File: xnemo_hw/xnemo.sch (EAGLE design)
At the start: 40 parts, among them J1 MICRO_USB_B_RECEPT, J2 DM3D_MICRO_SD, J3 HEADER_2X5_0.05_SMD, J4 HEADER_2X5_0.05_THRU, J5 HEADER_2X5_0.05_THRU, U1 LTC3559, U2 L3GD20, U3 STM32F405RG, U4 STM32F407VE, U5 HMC5883L, U6 ADXL345, X1 TXC_7A_XTAL

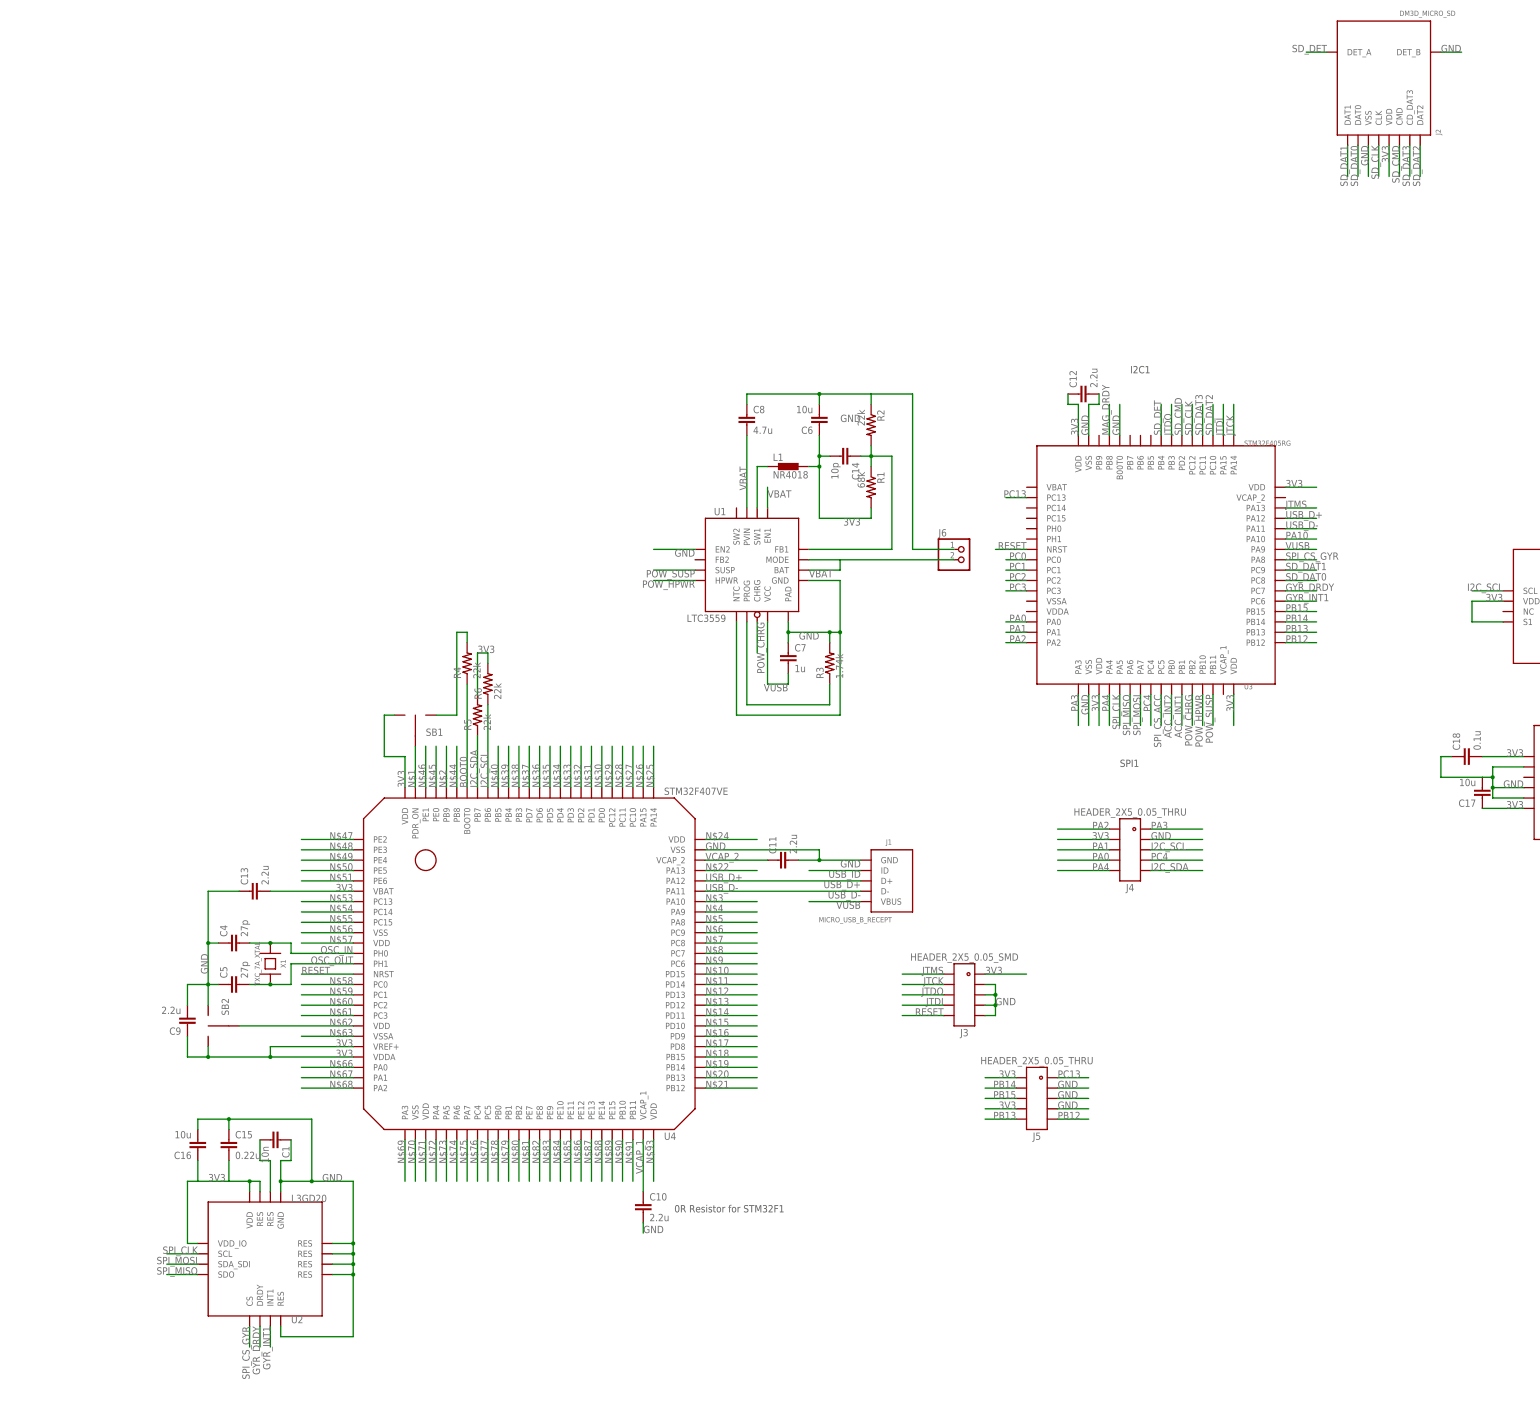
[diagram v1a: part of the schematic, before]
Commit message: More junk added -- 2 compass units...
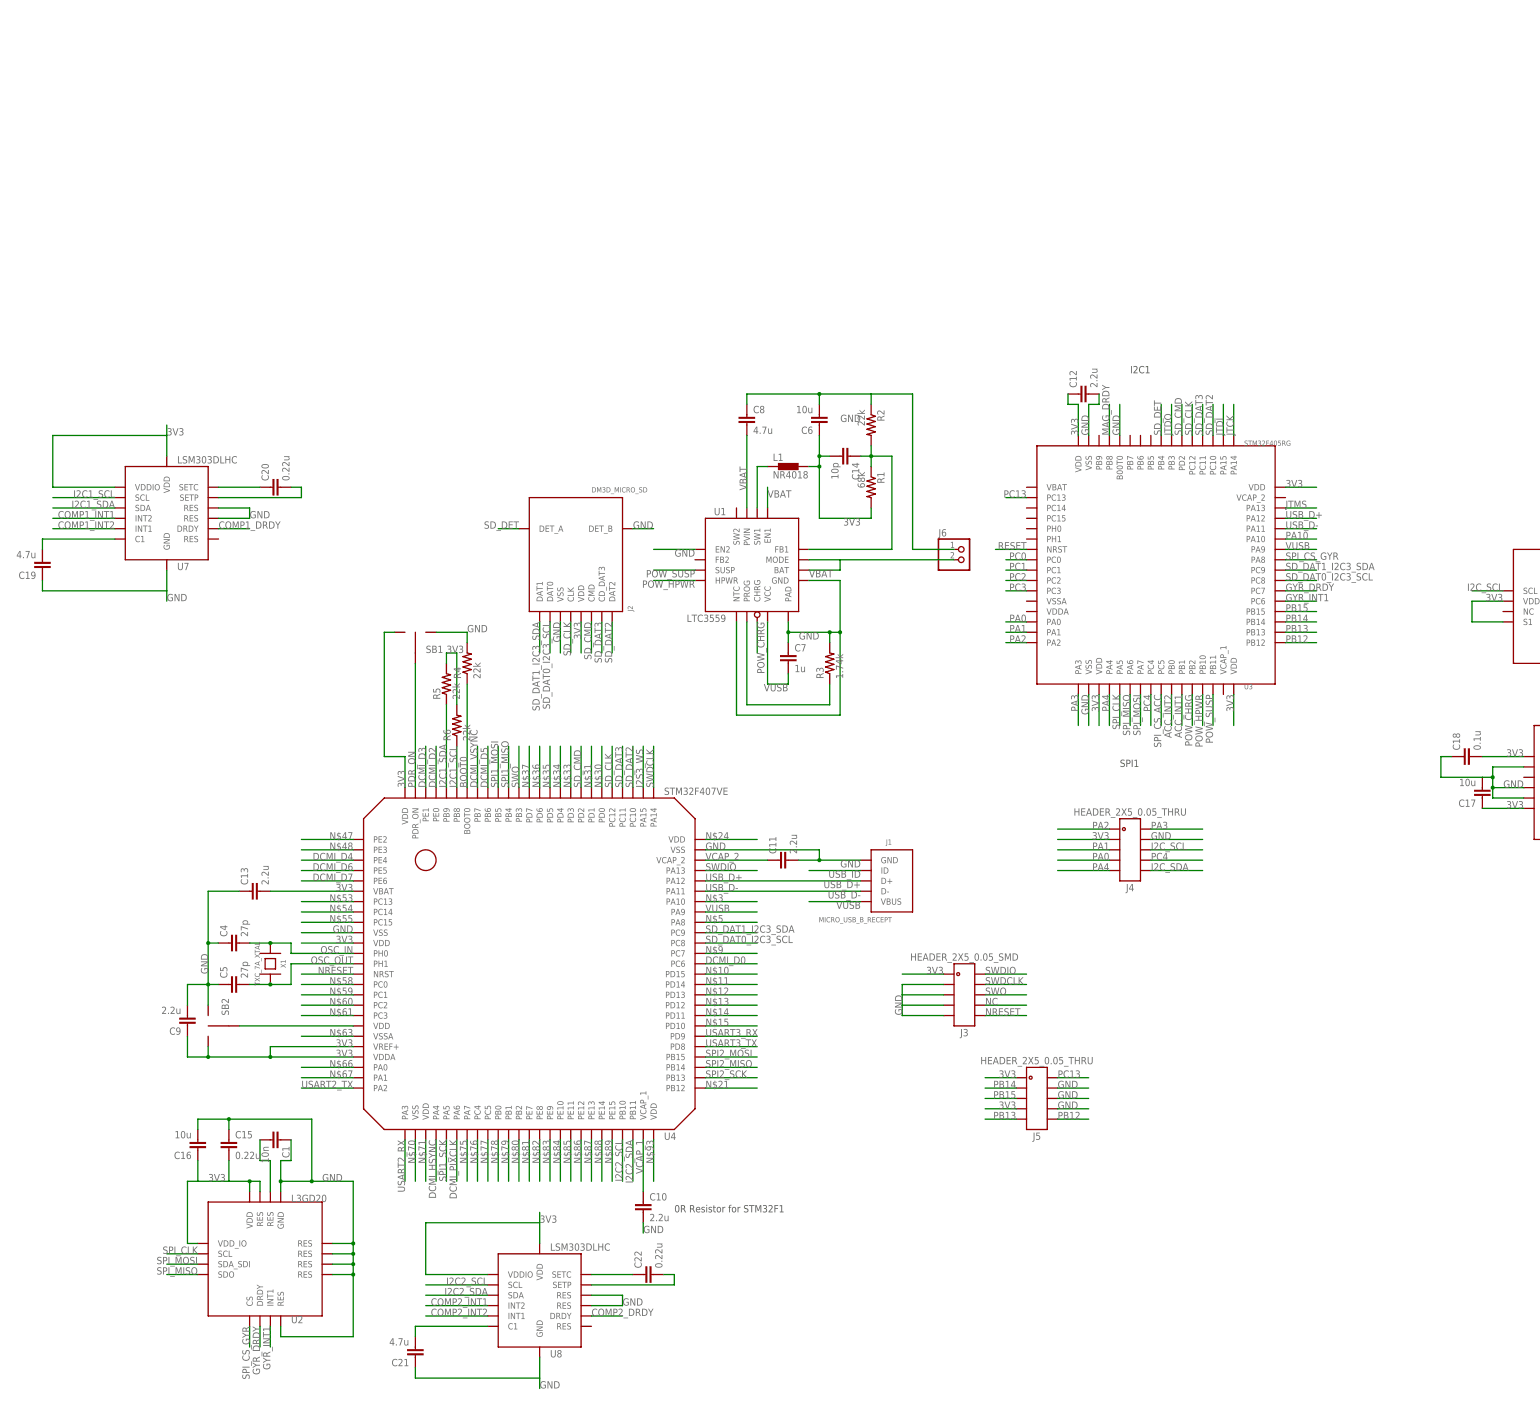
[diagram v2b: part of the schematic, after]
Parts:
- added C19, C21: 4.7u, resistor:C-EUC0805
- added C20, C22: 0.22u, resistor:C-EUC0402
- added U7, U8: LSM303DLHC, xnemo:LSM303DLHC
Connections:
- net N$1 renamed PDR_ON
- net N$16 renamed USART3_RX
- net N$17 renamed USART3_TX
- net N$18 renamed SPI2_MOSI
- net N$19 renamed SPI2_MISO
- net N$20 renamed SPI2_SCK
- net N$26 renamed I2S3_WS
- net N$39 renamed SPI1_MISO
- net N$40 renamed SPI1_MOSI
- net N$45 renamed DCMI_D2
- net N$46 renamed DCMI_D3
- net N$49 renamed DCMI_D4
- net N$50 renamed DCMI_D6
- net N$51 renamed DCMI_D7
- net N$68 renamed USART2_TX
- net N$69 renamed USART2_RX
- net N$72 renamed DCMI_HSYNC
- net N$73 renamed SPI1_SCK
- net N$74 renamed DCMI_PIXCLK
- net N$9 renamed DCMI_D0
- removed net N$2: U4.PB9
- removed net N$22: U4.PA13
- removed net N$25: U4.PA14
- removed net N$29: U4.PC12
- removed net N$32: U4.PD2
- removed net N$38: U4.PB3
- removed net N$4: U4.PA9
- removed net N$44: U4.PB8
- removed net N$56: U4.VSS@1
- removed net N$57: U4.VDD@1
- removed net N$90: U4.PB10
- removed net N$91: U4.PB11
- removed net SD_DAT0: J2.DAT0, U3.PC8
- removed net SD_DAT1: J2.DAT1, U3.PC9
- new net COMP1_DRDY: U7.DRDY
- new net COMP1_INT1: U7.INT2
- new net COMP1_INT2: U7.INT1
- new net COMP2_DRDY: U8.DRDY
- new net COMP2_INT1: U8.INT2
- new net COMP2_INT2: U8.INT1
- new net DCMI_D5: U4.PB6
- new net DCMI_VSYNC: U4.PB7
- new net I2C1_SCL: R6.1, U4.PB8, U7.SCL
- new net I2C1_SDA: R5.1, U4.PB9, U7.SDA
- new net I2C2_SCL: U4.PB10, U8.SCL
- new net I2C2_SDA: U4.PB11, U8.SDA
- new net N$23: C22.1, U8.SETC
- new net N$52: C19.2, U7.C1
- new net NC: J3.7
- new net NRESET: J3.9, U4.NRST
- new net SD_DAT0_I2C3_SCL: J2.DAT0, U3.PC8, U4.PC8
- new net SD_DAT1_I2C3_SDA: J2.DAT1, U3.PC9, U4.PC9
- new net SWDCLK: J3.3, U4.PA14
- new net SWDIO: J3.1, U4.PA13
- new net SWO: J3.5, U4.PB3
- net 3V3: now also J3.2, U4.VDD@1, U7.VDD, U7.VDDIO, U8.VDD, U8.VDDIO; no longer J3.1
- net GND: now also C19.1, C21.1, J3.10, J3.4, J3.6, J3.8, U4.VSS@1, U7.GND, U7.RES@2, U7.RES@3, U8.GND, U8.RES@2, U8.RES@3; no longer J3.3, J3.5, J3.7, J3.9
- net I2C_SCL: no longer R6.1, U4.PB6
- net I2C_SDA: no longer R5.1, U4.PB7
- net JTCK: no longer J3.4
- net JTDI: no longer J3.8
- net JTDO: no longer J3.6
- net JTMS: no longer J3.2
- net N$27: now also C20.1, U7.SETC; no longer U4.PC10
- net N$28: now also C21.2, U8.C1; no longer U4.PC11
- net N$6: now also C22.2, U8.SETP; no longer U4.PC9
- net N$7: now also C20.2, U7.SETP; no longer U4.PC8
- net RESET: no longer J3.10, U4.NRST
- net SD_CLK: now also U4.PC12
- net SD_CMD: now also U4.PD2
- net SD_DAT2: now also U4.PC10
- net SD_DAT3: now also U4.PC11
- net VUSB: now also U4.PA9
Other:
- moved on the sheet: J2, R5, R6, SB1

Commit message: Started routing
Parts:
- removed C18: 0.1u, resistor:C-EUC0402
- removed J5: HEADER_2X5_0.05_THRU, xnemo:HEADER_2X5_0.05_THRU
- removed U3: STM32F405RG, xnemo:STM32F405RG
- removed U5: HMC5883L, xnemo:HMC5883L
- removed U6: ADXL345, xnemo:ADXL345
- added C23: 10n, resistor:C-EUC0402
- added C24: 0.22u, resistor:C-EUC0402
- added C25: 10u, resistor:C-EUC0805
- added R7: 33k, resistor:R-US_R0402
- added R8, R9: 22k, resistor:R-US_R0402
- added U10: STTS751, xnemo:STTS751
- added U9: L3GD20, xnemo:L3GD20
- C17: value 10u -> 2.2u; device resistor:C-EUC0805 -> resistor:C-EUC0603
- C2: value 0.22u -> 10u; device resistor:C-EUC0402 -> resistor:C-EUC0805
- C3: value 4.7u -> 2.2u; device resistor:C-EUC0805 -> resistor:C-EUC0603
- J4: value HEADER_2X5_0.05_THRU -> HEADER_2X7; device xnemo:HEADER_2X5_0.05_THRU -> xnemo:HEADER_2X7
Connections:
- net GYR_RES renamed GYR_RES1
- net N$21 renamed SPI2_NSS_WS
- net N$28 renamed COMP2_C1
- net N$52 renamed COMP1_C1
- net SPI2_MISO renamed SPI2_MISO_EXT_SD
- net SPI2_MOSI renamed SPI2_MOSI_SD
- net SPI2_SCK renamed SPI2_SCK_CK
- removed net ACC_INT1: U3.PB1, U6.INT1
- removed net ACC_INT2: U3.PB0, U6.INT2
- removed net DCMI_D0: U4.PC6
- removed net GYR_DRDY: U2.DRDY, U3.PC7
- removed net GYR_INT1: U2.INT1, U3.PC6
- removed net I2C_SCL: J4.5, U5.SCL
- removed net I2C_SDA: J4.9, U5.SDA
- removed net JTCK: U3.PA14
- removed net JTDI: U3.PA15
- removed net JTDO: U3.PB3
- removed net JTMS: U3.PA13
- removed net MAG_C1: C3.1, U5.C1
- removed net MAG_DRDY: U3.PB8, U5.DRDY
- removed net MAG_SETC: C2.2, U5.SETC
- removed net MAG_SETP: C2.1, U5.SETP
- removed net N$24: U4.VDD@5
- removed net N$30: U4.PD0
- removed net N$31: U4.PD1
- removed net N$33: U4.PD3
- removed net N$34: U4.PD4
- removed net N$35: U4.PD5
- removed net N$36: U4.PD6
- removed net N$37: U4.PD7
- removed net N$59: U4.PC1
- removed net N$60: U4.PC2
- removed net N$61: U4.PC3
- removed net N$63: U4.VSSA
- removed net N$70: U4.VSS@2
- removed net N$71: U4.VDD@3
- removed net N$84: U4.PE10
- removed net N$85: U4.PE11
- removed net N$86: U4.PE12
- removed net N$87: U4.PE13
- removed net N$88: U4.PE14
- removed net N$89: U4.PE15
- removed net N$9: U4.PC7
- removed net N$93: U4.VDD@4
- removed net PA0: J4.8, U3.PA0
- removed net PA1: J4.6, U3.PA1
- removed net PA10: U3.PA10
- removed net PA2: J4.2, U3.PA2
- removed net PA3: J4.1, U3.PA3
- removed net PA4: J4.10, U3.PA4
- removed net PB12: J5.9, U3.PB12
- removed net PB13: J5.10, U3.PB13
- removed net PB14: J5.4, U3.PB14
- removed net PB15: J5.6, U3.PB15
- removed net PC0: U3.PC0
- removed net PC1: U3.PC1
- removed net PC13: J5.1, U3.PC13
- removed net PC2: U3.PC2
- removed net PC3: U3.PC3
- removed net PC4: J4.7, U3.PC4
- removed net RESET: U3.NRST
- removed net SPI_CLK: U2.SCL, U3.PA5, U6.SCL
- removed net SPI_CS_ACC: U3.PC5, U6.NCS
- removed net SPI_CS_GYR: U2.CS, U3.PA8
- removed net SPI_MISO: U2.SDO, U3.PA6, U6.SDO
- removed net SPI_MOSI: U2.SDA_SDI, U3.PA7, U6.SDI
- new net DCMI_D0_MCK: J4.4, U4.PC6
- new net DCMI_D1: J4.6, U4.PC7
- new net GYR1_DRDY: U2.DRDY, U4.PC2
- new net GYR1_INT1: U2.INT1, U4.PC3
- new net GYR2_DRDY: U4.PE14, U9.DRDY
- new net GYR2_INT1: U4.PE13, U9.INT1
- new net GYR_RES2: C23.2, U9.RES@6
- new net SPI_CS_GYR1: U2.CS, U4.PC1
- new net SPI_CS_GYR2: U4.PE15, U9.CS
- new net TEMP1_ADDR: R7.1, U10.ADR
- new net TEMP1_EVT: U10.EVT
- net 3V3: now also C17.2, C2.1, C24.2, C25.1, C3.1, J4.11, R7.2, R8.2, R9.2, U10.VDD, U4.VDD@3, U4.VDD@4, U4.VDD@5, U9.RES@7, U9.VDD, U9.VDD_IO; no longer C17.1, C18.2, J4.4, J5.2, J5.8, U3.VDD@1, U3.VDD@2, U3.VDD@3, U3.VDD@4, U5.S1, U5.VDD, U5.VDDIO, U6.VDDIO, U6.VS
- net COMP1_DRDY: now also U4.PD7
- net COMP1_INT1: now also U4.PD5
- net COMP1_INT2: now also U4.PD6
- net COMP2_DRDY: now also U4.PE10
- net COMP2_INT1: now also U4.PE12
- net COMP2_INT2: now also U4.PE11
- net DCMI_D2: now also J4.8
- net DCMI_D3: now also J4.10
- net DCMI_D4: now also J4.12
- net DCMI_D5: now also J4.14
- net DCMI_D6: now also J4.1
- net DCMI_D7: now also J4.3
- net DCMI_HSYNC: now also J4.9
- net DCMI_PIXCLK: now also J4.5
- net DCMI_VSYNC: now also J4.7
- net GND: now also C17.1, C2.2, C23.1, C24.1, C25.2, J4.13, J4.2, U10.GND, U4.VSS@2, U4.VSSA, U9.GND, U9.RES@1, U9.RES@2, U9.RES@3, U9.RES@4, U9.RES@5; no longer C17.2, C18.1, J4.3, J5.3, J5.5, J5.7, U3.B00T0, U3.VSS@1, U3.VSS@2, U5.GND@1, U5.GND@2, U6.GND@1, U6.GND@2, U6.GND@3
- net I2C1_SCL: now also U10.SCL
- net I2C1_SDA: now also U10.SDA
- net I2C2_SCL: now also R9.1
- net I2C2_SDA: now also R8.1
- net POW_CHRG: now also U4.PD0; no longer U3.PB2
- net POW_HPWR: now also U4.PD1; no longer U3.PB10
- net POW_SUSP: now also U4.PD4; no longer U3.PB11
- net SD_CLK: no longer U3.PC12
- net SD_CMD: no longer U3.PD2
- net SD_DAT0_I2C3_SCL: no longer U3.PC8
- net SD_DAT1_I2C3_SDA: no longer U3.PC9
- net SD_DAT2: no longer U3.PC10
- net SD_DAT3: no longer U3.PC11
- net SD_DET: now also U4.PD3; no longer U3.PB4
- net SPI1_MISO: now also U2.SDO, U9.SDO
- net SPI1_MOSI: now also U2.SDA_SDI, U9.SDA_SDI
- net SPI1_SCK: now also U2.SCL, U9.SCL
- net USB_D+: no longer U3.PA12
- net USB_D-: no longer U3.PA11
- net VUSB: no longer U3.PA9
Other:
- note added: "DCMI Header"
- note removed: "I2C1"
- note removed: "SPI1"
- moved on the sheet: C12, C17, C19, C2, C21, C3
